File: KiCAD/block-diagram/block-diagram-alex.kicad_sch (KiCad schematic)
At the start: 16 parts, among them Q3 NMOS, Q4 NMOS, SW1 SW_Push, SW2 SW, SW3 SW, SW4 SW_SPST, U1 74LS02, U2 74LS02, U3 74LS11, U6 LMC555xM

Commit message: trying to fix issues
Issues with merging are preventing me to pull origin
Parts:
- removed unit 3 of U1
- renumbered U2 to U1
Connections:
- net at U3.13: now also U1.10; no longer U1.1
- net at R3.2: now also U1.8; no longer U1.2
- net at R4.2, SW4.2 (B): now also U1.9; no longer U1.3
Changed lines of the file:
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@@
 		)
 		(instances
-			(project "block-diagram"
+			(project "block-diagram-alex"
 				(path "/db38bfac-663c-442a-8ac2-f7bf1aa9a3fd"
 					(reference "SW2")
@@
 		)
 		(instances
-			(project "block-diagram"
+			(project "block-diagram-alex"
 				(path "/db38bfac-663c-442a-8ac2-f7bf1aa9a3fd"
 					(reference "#PWR011")
@@
 		)
 		(instances
-			(project "block-diagram"
+			(project "block-diagram-alex"
 				(path "/db38bfac-663c-442a-8ac2-f7bf1aa9a3fd"
 					(reference "#PWR07")
@@
 		)
 		(instances
-			(project "block-diagram"
+			(project "block-diagram-alex"
 				(path "/db38bfac-663c-442a-8ac2-f7bf1aa9a3fd"
 					(reference "U1")
@@
 		)
 		(instances
-			(project "block-diagram"
+			(project "block-diagram-alex"
 				(path "/db38bfac-663c-442a-8ac2-f7bf1aa9a3fd"
 					(reference "U6")
@@
 		(lib_id "74xx:74LS02")
 		(at 213.36 121.92 0)
-		(unit 1)
-		(exclude_from_sim no)
-		(in_bom yes)
-		(on_board yes)
-		(dnp no)
-		(property "Reference" "U2"
+		(unit 3)
+		(exclude_from_sim no)
+		(in_bom yes)
+		(on_board yes)
+		(dnp no)
+		(property "Reference" "U1"
 			(at 208.28 116.078 0)
 			(effects
@@
 		)
 		(instances
-			(project "block-diagram"
-				(path "/db38bfac-663c-442a-8ac2-f7bf1aa9a3fd"
-					(reference "U2")
-					(unit 1)
+			(project "block-diagram-alex"
+				(path "/db38bfac-663c-442a-8ac2-f7bf1aa9a3fd"
+					(reference "U1")
+					(unit 3)
 				)
 			)
@@
 		)
 		(instances
-			(project "block-diagram"
+			(project "block-diagram-alex"
 				(path "/db38bfac-663c-442a-8ac2-f7bf1aa9a3fd"
 					(reference "#PWR05")
@@
 		)
 		(instances
-			(project "block-diagram"
+			(project "block-diagram-alex"
 				(path "/db38bfac-663c-442a-8ac2-f7bf1aa9a3fd"
 					(reference "U1")
@@
 		)
 		(instances
-			(project "block-diagram"
+			(project "block-diagram-alex"
 				(path "/db38bfac-663c-442a-8ac2-f7bf1aa9a3fd"
 					(reference "#PWR015")
 					(unit 1)
-				)
-			)
-		)
-	)
-	(symbol
-		(lib_id "74xx:74LS02")
-		(at 231.14 151.13 0)
-		(unit 3)
-		(exclude_from_sim no)
-		(in_bom yes)
-		(on_board yes)
-		(dnp no)
-		(fields_autoplaced yes)
-		(property "Reference" "U1"
-			(at 231.14 142.24 0)
-			(effects
-				(font
-					(size 1.27 1.27)
-				)
-			)
-		)
-		(property "Value" "74LS02"
-			(at 231.14 144.78 0)
-			(effects
-				(font
-					(size 1.27 1.27)
-				)
-			)
-		)
-		(property "Footprint" "Package_SO:SOIC-14_3.9x8.7mm_P1.27mm"
-			(at 231.14 151.13 0)
-			(effects
-				(font
-					(size 1.27 1.27)
-				)
-				(hide yes)
-			)
-		)
-		(property "Datasheet" "http://www.ti.com/lit/gpn/sn74ls02"
-			(at 231.14 151.13 0)
-			(effects
-				(font
-					(size 1.27 1.27)
-				)
-				(hide yes)
-			)
-		)
-		(property "Description" "quad 2-input NOR gate"
-			(at 231.14 151.13 0)
-			(effects
-				(font
-					(size 1.27 1.27)
-				)
-				(hide yes)
-			)
-		)
-		(pin "11"
-		)
-		(pin "6"
-		)
-		(pin "14"
-		)
-		(pin "13"
-		)
-		(pin "2"
-		)
-		(pin "12"
-		)
-		(pin "7"
-		)
-		(pin "1"
-		)
-		(pin "3"
-		)
-		(pin "4"
-		)
-		(pin "10"
-		)
-		(pin "8"
-		)
-		(pin "9"
-		)
-		(pin "5"
-		)
-		(instances
-			(project "block-diagram"
-				(path "/db38bfac-663c-442a-8ac2-f7bf1aa9a3fd"
-					(reference "U1")
-					(unit 3)
 				)
 			)
@@
 		)
 		(instances
-			(project "block-diagram"
+			(project "block-diagram-alex"
 				(path "/db38bfac-663c-442a-8ac2-f7bf1aa9a3fd"
 					(reference "U3")
@@
 		)
 		(instances
-			(project "block-diagram"
+			(project "block-diagram-alex"
 				(path "/db38bfac-663c-442a-8ac2-f7bf1aa9a3fd"
 					(reference "C3")
@@
 		)
 		(instances
-			(project "block-diagram"
+			(project "block-diagram-alex"
 				(path "/db38bfac-663c-442a-8ac2-f7bf1aa9a3fd"
 					(reference "#PWR010")
@@
 		)
 		(instances
-			(project "block-diagram"
+			(project "block-diagram-alex"
 				(path "/db38bfac-663c-442a-8ac2-f7bf1aa9a3fd"
 					(reference "SW3")
@@
 		)
 		(instances
-			(project "block-diagram"
+			(project "block-diagram-alex"
 				(path "/db38bfac-663c-442a-8ac2-f7bf1aa9a3fd"
 					(reference "U1")
@@
 		)
 		(instances
-			(project "block-diagram"
+			(project "block-diagram-alex"
 				(path "/db38bfac-663c-442a-8ac2-f7bf1aa9a3fd"
 					(reference "#PWR04")
@@
 		)
 		(instances
-			(project "block-diagram"
+			(project "block-diagram-alex"
 				(path "/db38bfac-663c-442a-8ac2-f7bf1aa9a3fd"
 					(reference "#PWR01")
@@
 		)
 		(instances
-			(project "block-diagram"
+			(project "block-diagram-alex"
 				(path "/db38bfac-663c-442a-8ac2-f7bf1aa9a3fd"
 					(reference "#PWR02")
@@
 		)
 		(instances
-			(project "block-diagram"
+			(project "block-diagram-alex"
 				(path "/db38bfac-663c-442a-8ac2-f7bf1aa9a3fd"
 					(reference "#PWR014")
@@
 		)
 		(instances
-			(project "block-diagram"
+			(project "block-diagram-alex"
 				(path "/db38bfac-663c-442a-8ac2-f7bf1aa9a3fd"
 					(reference "#PWR03")
@@
 		)
 		(instances
-			(project "block-diagram"
+			(project "block-diagram-alex"
 				(path "/db38bfac-663c-442a-8ac2-f7bf1aa9a3fd"
 					(reference "#PWR013")
@@
 		)
 		(instances
-			(project "block-diagram"
+			(project "block-diagram-alex"
 				(path "/db38bfac-663c-442a-8ac2-f7bf1aa9a3fd"
 					(reference "R3")
@@
 		)
 		(instances
-			(project "block-diagram"
+			(project "block-diagram-alex"
 				(path "/db38bfac-663c-442a-8ac2-f7bf1aa9a3fd"
 					(reference "U1")
@@
 		)
 		(instances
-			(project "block-diagram"
+			(project "block-diagram-alex"
 				(path "/db38bfac-663c-442a-8ac2-f7bf1aa9a3fd"
 					(reference "#PWR012")
@@
 		)
 		(instances
-			(project "block-diagram"
+			(project "block-diagram-alex"
 				(path "/db38bfac-663c-442a-8ac2-f7bf1aa9a3fd"
 					(reference "U3")
@@
 		)
 		(instances
-			(project "block-diagram"
+			(project "block-diagram-alex"
 				(path "/db38bfac-663c-442a-8ac2-f7bf1aa9a3fd"
 					(reference "R2")
@@
 		)
 		(instances
-			(project "block-diagram"
+			(project "block-diagram-alex"
 				(path "/db38bfac-663c-442a-8ac2-f7bf1aa9a3fd"
 					(reference "Q4")
@@
 		)
 		(instances
-			(project "block-diagram"
+			(project "block-diagram-alex"
 				(path "/db38bfac-663c-442a-8ac2-f7bf1aa9a3fd"
 					(reference "C4")
@@
 		)
 		(instances
-			(project "block-diagram"
+			(project "block-diagram-alex"
 				(path "/db38bfac-663c-442a-8ac2-f7bf1aa9a3fd"
 					(reference "U3")
@@
 		)
 		(instances
-			(project "block-diagram"
+			(project "block-diagram-alex"
 				(path "/db38bfac-663c-442a-8ac2-f7bf1aa9a3fd"
 					(reference "#PWR06")
@@
 		)
 		(instances
-			(project "block-diagram"
+			(project "block-diagram-alex"
 				(path "/db38bfac-663c-442a-8ac2-f7bf1aa9a3fd"
 					(reference "R1")
@@
 		)
 		(instances
-			(project "block-diagram"
+			(project "block-diagram-alex"
 				(path "/db38bfac-663c-442a-8ac2-f7bf1aa9a3fd"
 					(reference "R4")
@@
 		)
 		(instances
-			(project "block-diagram"
+			(project "block-diagram-alex"
 				(path "/db38bfac-663c-442a-8ac2-f7bf1aa9a3fd"
 					(reference "SW1")
@@
 		)
 		(instances
-			(project "block-diagram"
+			(project "block-diagram-alex"
 				(path "/db38bfac-663c-442a-8ac2-f7bf1aa9a3fd"
 					(reference "U3")
@@
 		)
 		(instances
-			(project "block-diagram"
+			(project "block-diagram-alex"
 				(path "/db38bfac-663c-442a-8ac2-f7bf1aa9a3fd"
 					(reference "Q3")
@@
 		)
 		(instances
-			(project "block-diagram"
+			(project "block-diagram-alex"
 				(path "/db38bfac-663c-442a-8ac2-f7bf1aa9a3fd"
 					(reference "SW4")

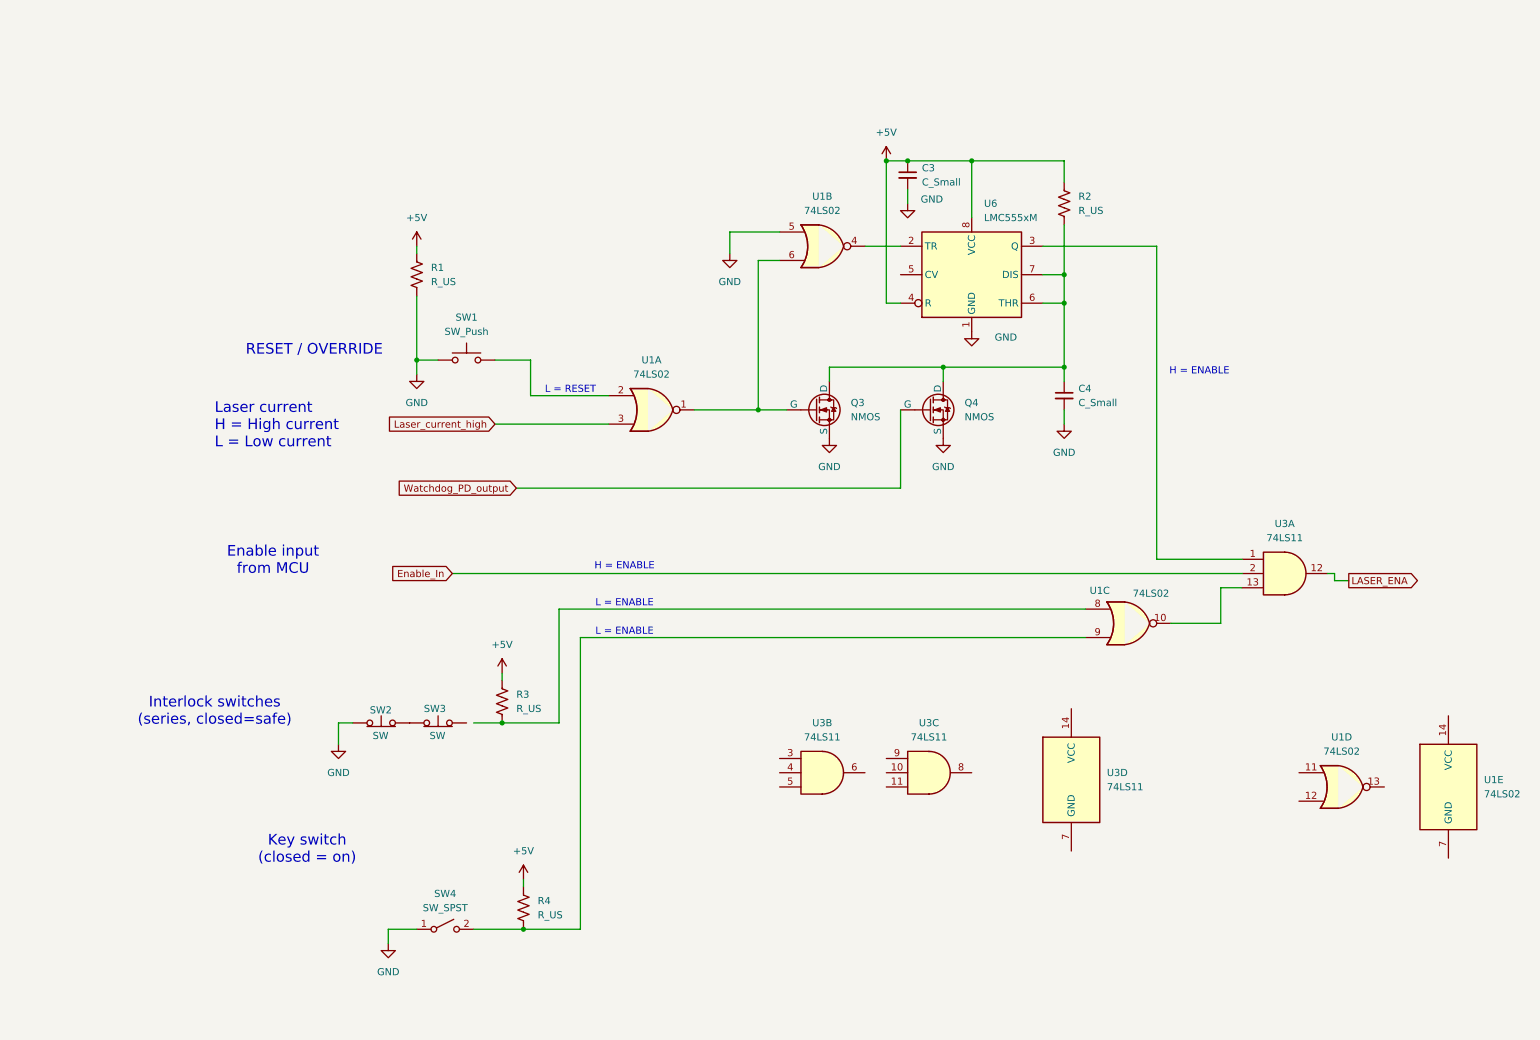
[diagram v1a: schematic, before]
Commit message: Schematic Updates
Added 8 pin connectors. Connected power and ground to logic chips. Added capacitor and ground to the +5V for ICs. For unused logic gates, inputs tied to ground. No footprint assigned to 8 pin connectors yet.
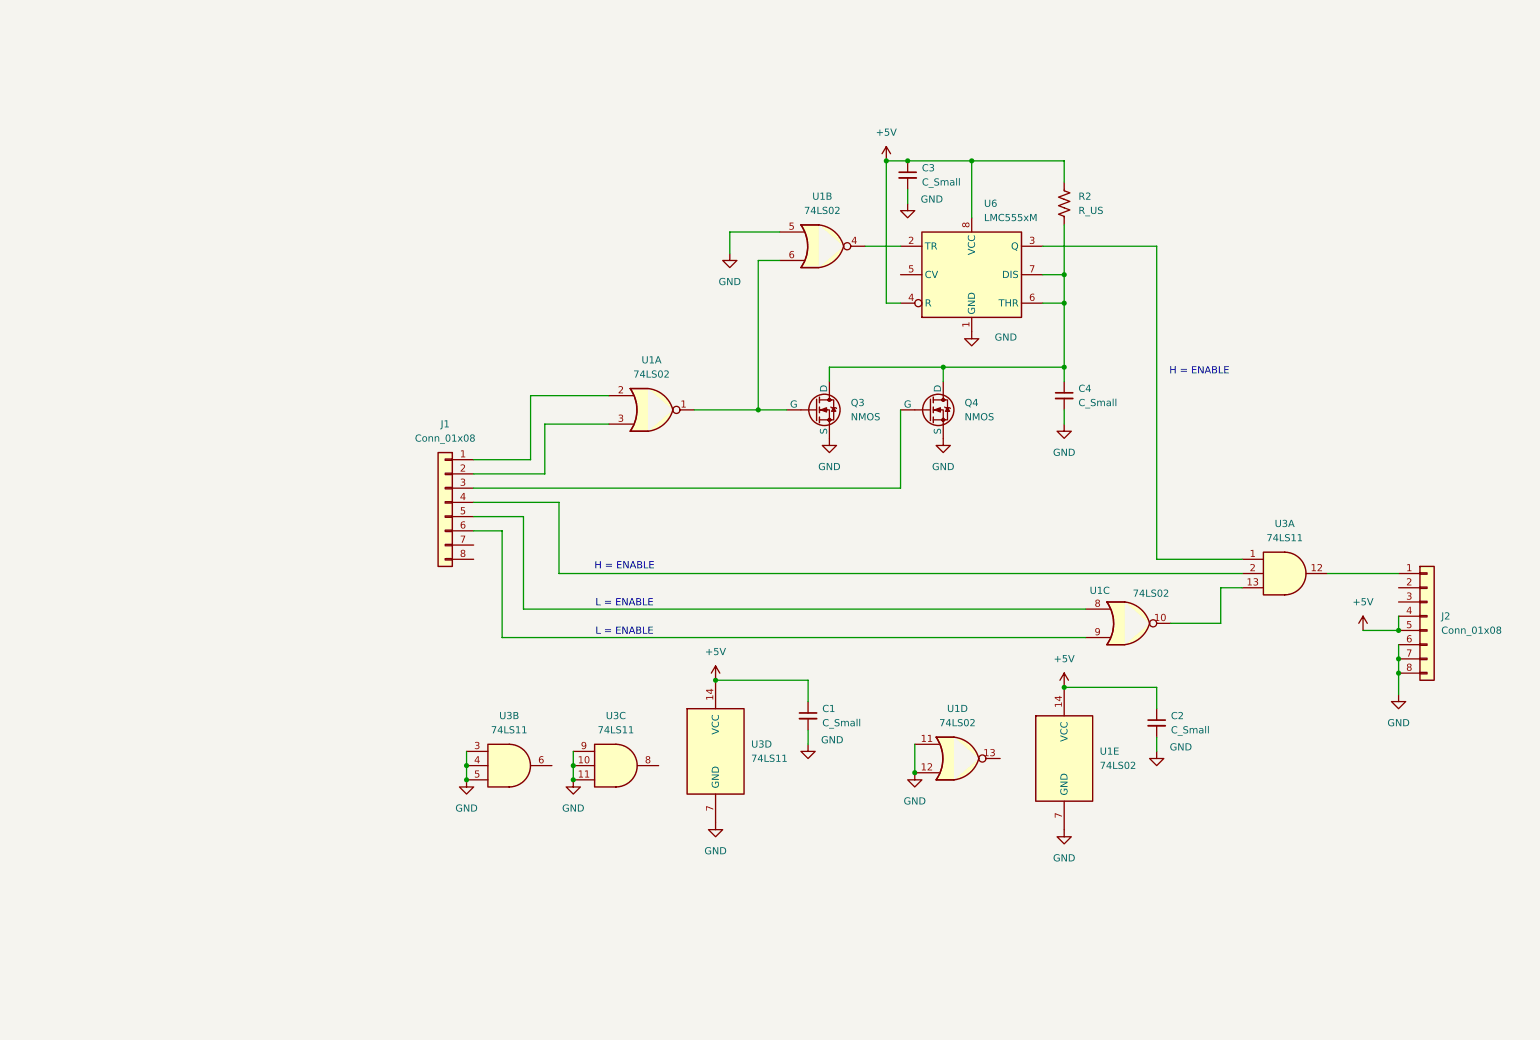
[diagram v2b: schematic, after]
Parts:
- removed R1, R3, R4: R_US, Resistor_SMD:R_1206_3216Metric, symbol Device:R_US
- removed SW1: SW_Push, symbol Switch:SW_Push
- removed SW2, SW3: SW, symbol Switch:SW_Push_Open
- removed SW4: SW_SPST, symbol Switch:SW_SPST
- added C1, C2: C_Small, Capacitor_SMD:C_1206_3216Metric, symbol Device:C_Small
- added J1, J2: Conn_01x08, symbol Connector_Generic:Conn_01x08
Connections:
- net +5V: now also U1.14 (VCC), U3.14 (VCC), C1.1, C2.1, J2.4 (Pin_4), J2.5 (Pin_5)
- net GND: now also U1.11, U1.12, U1.7 (GND), U3.10, U3.11, U3.3, U3.4, U3.5, U3.7 (GND), U3.9, C1.2, C2.2, J2.6 (Pin_6), J2.7 (Pin_7), J2.8 (Pin_8)
- net at U1.8: now also J1.5 (Pin_5)
- net at U1.9: now also J1.6 (Pin_6)
- net at U1.2: now also J1.1 (Pin_1)
- net Enable_In: no longer names the net of U3.2
- net Enable_In: now also J1.4 (Pin_4)
- net LASER_ENA: no longer names the net of U3.12
- net LASER_ENA: now also J2.1 (Pin_1)
- net Laser_current_high: no longer names the net of U1.3
- net Laser_current_high: now also J1.2 (Pin_2)
- net Watchdog_PD_output: no longer names the net of Q4.2 (G)
- net Watchdog_PD_output: now also J1.3 (Pin_3)
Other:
- note removed: "Enable input from MCU"
- note removed: "Interlock switches (series, closed=safe)"
- note removed: "Key switch (closed = on)"
- note removed: "L = RESET"
- note removed: "Laser current H = High current L = Low current"
- note removed: "RESET / OVERRIDE"
- moved on the sheet: U1D, U1E, U3B, U3C, U3D

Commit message: tentative placement, add test points and LEDs
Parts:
- added D1, D2, D3, D4, D5, D6, D7, D8: LED, LED_SMD:LED_1206_3216Metric_Pad1.42x1.75mm_HandSolder, symbol Device:LED
- added H1, H2, H3, H4: MountingHole_Pad, my_mtg_hole:hole_250_150, symbol Mechanical:MountingHole_Pad
- added J3: Conn_01x10, Connector_PinSocket_2.54mm:PinSocket_1x10_P2.54mm_Vertical, symbol Connector_Generic:Conn_01x10
- added R1: 470, Resistor_SMD:R_1206_3216Metric_Pad1.30x1.75mm_HandSolder, symbol Device:R_US
- added R3, R4, R5, R6, R7, R8, R9: 470, Resistor_SMD:R_1206_3216Metric, symbol Device:R_US
- J1, J2: footprint (none) -> Connector_PinHeader_2.54mm:PinHeader_1x08_P2.54mm_Vertical
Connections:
- net GND: now also D1.1 (K), D2.1 (K), D3.1 (K), D4.1 (K), D5.1 (K), D6.1 (K), D7.1 (K), D8.1 (K), H1.1, H2.1, H3.1, H4.1, J3.10 (Pin_10), J3.9 (Pin_9)
- net LASER_ENA: now reaches J2.1 (Pin_1), U3.12
- net LASER_ENA: now also J3.1 (Pin_1), R9.1
- net WDT_OUT: now reaches U3.1, U6.3 (Q)
- net WDT_OUT: now also J3.2 (Pin_2), R8.1
- net INTERLOCK: now reaches J1.5 (Pin_5), U1.8
- net INTERLOCK: now also J3.4 (Pin_4), R6.1
- net KEY_SW: now reaches J1.6 (Pin_6), U1.9
- net KEY_SW: now also J3.3 (Pin_3), R7.1
- net OVERRIDE: now reaches J1.1 (Pin_1), U1.2
- net OVERRIDE: now also J3.8 (Pin_8), R3.1
- net LC_HIGH: now reaches J1.2 (Pin_2), U1.3
- net LC_HIGH: now also J3.7 (Pin_7), R1.1
- net MCU_ENA: now reaches J1.4 (Pin_4), U3.2
- net MCU_ENA: now also J3.5 (Pin_5), R5.1
- net WD_PHOTODIODE: now reaches J1.3 (Pin_3), Q4.2 (G)
- net WD_PHOTODIODE: now also J3.6 (Pin_6), R4.1
- new net: D3.2 (A), R4.2
- new net: D7.2 (A), R8.2
- new net: D1.2 (A), R1.2
- new net: D6.2 (A), R7.2
- new net: D4.2 (A), R5.2
- new net: D8.2 (A), R9.2
- new net: D5.2 (A), R6.2
- new net: D2.2 (A), R3.2
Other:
- moved on the sheet: C1, C2, C3, C4, J1, J2, Q3, Q4, R2, U1A, U1B, U1C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

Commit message: add LEDs and test connector, update placement
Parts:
- C1, C2, C3, C4: footprint Capacitor_SMD:C_1206_3216Metric -> Capacitor_SMD:C_0805_2012Metric_Pad1.18x1.45mm_HandSolder
- D1, D2, D3, D4, D5, D6, D7, D8: footprint LED_SMD:LED_1206_3216Metric_Pad1.42x1.75mm_HandSolder -> LED_SMD:LED_0805_2012Metric_Pad1.15x1.40mm_HandSolder
- R1: footprint Resistor_SMD:R_1206_3216Metric_Pad1.30x1.75mm_HandSolder -> Resistor_SMD:R_0805_2012Metric_Pad1.20x1.40mm_HandSolder
- R2, R3, R4, R5, R6, R7, R8, R9: footprint Resistor_SMD:R_1206_3216Metric -> Resistor_SMD:R_0805_2012Metric_Pad1.20x1.40mm_HandSolder
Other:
- note added: "Testpoints"
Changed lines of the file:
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@@
 		)
 	)
+	(text "Testpoints"
+		(exclude_from_sim no)
+		(at 152.908 163.068 0)
+		(effects
+			(font
+				(size 1.27 1.27)
+			)
+		)
+	)
 	(text "L = ENABLE"
 		(exclude_from_sim no)
@@
 			)
 		)
-		(property "Footprint" "Resistor_SMD:R_1206_3216Metric"
+		(property "Footprint" "Resistor_SMD:R_0805_2012Metric_Pad1.20x1.40mm_HandSolder"
 			(at 105.156 178.054 90)
 			(effects
@@
 			)
 		)
-		(property "Footprint" "LED_SMD:LED_1206_3216Metric_Pad1.42x1.75mm_HandSolder"
+		(property "Footprint" "LED_SMD:LED_0805_2012Metric_Pad1.15x1.40mm_HandSolder"
 			(at 92.71 158.75 0)
 			(effects
@@
 			)
 		)
-		(property "Footprint" "Capacitor_SMD:C_1206_3216Metric"
+		(property "Footprint" "Capacitor_SMD:C_0805_2012Metric_Pad1.18x1.45mm_HandSolder"
 			(at 166.37 121.92 0)
 			(effects
@@
 			)
 		)
-		(property "Footprint" "Resistor_SMD:R_1206_3216Metric_Pad1.30x1.75mm_HandSolder"
+		(property "Footprint" "Resistor_SMD:R_0805_2012Metric_Pad1.20x1.40mm_HandSolder"
 			(at 105.156 183.134 90)
 			(effects
@@
 			)
 		)
-		(property "Footprint" "LED_SMD:LED_1206_3216Metric_Pad1.42x1.75mm_HandSolder"
+		(property "Footprint" "LED_SMD:LED_0805_2012Metric_Pad1.15x1.40mm_HandSolder"
 			(at 92.71 163.83 0)
 			(effects
@@
 			)
 		)
-		(property "Footprint" "LED_SMD:LED_1206_3216Metric_Pad1.42x1.75mm_HandSolder"
+		(property "Footprint" "LED_SMD:LED_0805_2012Metric_Pad1.15x1.40mm_HandSolder"
 			(at 92.71 184.15 0)
 			(effects
@@
 			)
 		)
-		(property "Footprint" "Capacitor_SMD:C_1206_3216Metric"
+		(property "Footprint" "Capacitor_SMD:C_0805_2012Metric_Pad1.18x1.45mm_HandSolder"
 			(at 184.15 25.4 0)
 			(effects
@@
 			)
 		)
-		(property "Footprint" "Capacitor_SMD:C_1206_3216Metric"
+		(property "Footprint" "Capacitor_SMD:C_0805_2012Metric_Pad1.18x1.45mm_HandSolder"
 			(at 228.6 123.19 0)
 			(effects
@@
 			)
 		)
-		(property "Footprint" "LED_SMD:LED_1206_3216Metric_Pad1.42x1.75mm_HandSolder"
+		(property "Footprint" "LED_SMD:LED_0805_2012Metric_Pad1.15x1.40mm_HandSolder"
 			(at 92.71 173.99 0)
 			(effects
@@
 			)
 		)
-		(property "Footprint" "LED_SMD:LED_1206_3216Metric_Pad1.42x1.75mm_HandSolder"
+		(property "Footprint" "LED_SMD:LED_0805_2012Metric_Pad1.15x1.40mm_HandSolder"
 			(at 92.71 179.07 0)
 			(effects
@@
 			)
 		)
-		(property "Footprint" "Resistor_SMD:R_1206_3216Metric"
+		(property "Footprint" "Resistor_SMD:R_0805_2012Metric_Pad1.20x1.40mm_HandSolder"
 			(at 105.156 152.654 90)
 			(effects
@@
 			)
 		)
-		(property "Footprint" "Resistor_SMD:R_1206_3216Metric"
+		(property "Footprint" "Resistor_SMD:R_0805_2012Metric_Pad1.20x1.40mm_HandSolder"
 			(at 105.156 172.974 90)
 			(effects
@@
 			)
 		)
-		(property "Footprint" "LED_SMD:LED_1206_3216Metric_Pad1.42x1.75mm_HandSolder"
+		(property "Footprint" "LED_SMD:LED_0805_2012Metric_Pad1.15x1.40mm_HandSolder"
 			(at 92.71 168.91 0)
 			(effects
@@
 			)
 		)
-		(property "Footprint" "Resistor_SMD:R_1206_3216Metric"
+		(property "Footprint" "Resistor_SMD:R_0805_2012Metric_Pad1.20x1.40mm_HandSolder"
 			(at 213.106 30.734 90)
 			(effects
@@
 			)
 		)
-		(property "Footprint" "LED_SMD:LED_1206_3216Metric_Pad1.42x1.75mm_HandSolder"
+		(property "Footprint" "LED_SMD:LED_0805_2012Metric_Pad1.15x1.40mm_HandSolder"
 			(at 92.71 153.67 0)
 			(effects
@@
 			)
 		)
-		(property "Footprint" "Resistor_SMD:R_1206_3216Metric"
+		(property "Footprint" "Resistor_SMD:R_0805_2012Metric_Pad1.20x1.40mm_HandSolder"
 			(at 105.156 188.214 90)
 			(effects
@@
 			)
 		)
-		(property "Footprint" "Capacitor_SMD:C_1206_3216Metric"
+		(property "Footprint" "Capacitor_SMD:C_0805_2012Metric_Pad1.18x1.45mm_HandSolder"
 			(at 212.09 64.77 0)
 			(effects
@@
 			)
 		)
-		(property "Footprint" "LED_SMD:LED_1206_3216Metric_Pad1.42x1.75mm_HandSolder"
+		(property "Footprint" "LED_SMD:LED_0805_2012Metric_Pad1.15x1.40mm_HandSolder"
 			(at 92.71 189.23 0)
 			(effects
@@
 			)
 		)
-		(property "Footprint" "Resistor_SMD:R_1206_3216Metric"
+		(property "Footprint" "Resistor_SMD:R_0805_2012Metric_Pad1.20x1.40mm_HandSolder"
 			(at 105.156 162.814 90)
 			(effects
@@
 			)
 		)
-		(property "Footprint" "Resistor_SMD:R_1206_3216Metric"
+		(property "Footprint" "Resistor_SMD:R_0805_2012Metric_Pad1.20x1.40mm_HandSolder"
 			(at 105.156 157.734 90)
 			(effects
@@
 			)
 		)
-		(property "Footprint" "Resistor_SMD:R_1206_3216Metric"
+		(property "Footprint" "Resistor_SMD:R_0805_2012Metric_Pad1.20x1.40mm_HandSolder"
 			(at 105.156 167.894 90)
 			(effects
